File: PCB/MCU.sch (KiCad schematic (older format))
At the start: 17 parts, among them SW1 EG1224, U1 STM32F767VIT6

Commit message: Changed PCB.
- Added MOSFET, connectors sheet
- Changed MCU and power sheet
- Reorganised sheets
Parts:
- added C? (x2): 8pF, Capacitor_SMD:C_0603_1608Metric, symbol Device:C
- added C? (x4): 100nF, Capacitor_SMD:C_0603_1608Metric, symbol Device:C
- added C? (x2): C, Capacitor_SMD:C_0603_1608Metric, symbol Device:C
- added L? (x2): MPZ1608S221A, Resistor_SMD:R_0603_1608Metric, symbol Device:Ferrite_Bead_Small
- added R? (x4): 22, Resistor_SMD:R_0603_1608Metric, symbol Device:R
- added R? (x4): 1K, Resistor_SMD:R_0603_1608Metric, symbol Device:R
- added R?: 10k, Resistor_SMD:R_0603_1608Metric, symbol Device:R
- added SW?: PTS645VL39-2, Button_Switch_THT:SW_Tactile_SPST_Angled_PTS645Vx39-2LFS, symbol Switch:SW_Push
- added TP?: MCO, symbol Connector_Specialized:Test_Point
- added TP?: CLK24, symbol Connector_Specialized:Test_Point
- added U?: ADUM4160, Package_SO:SOIC-16W_7.5x10.3mm_P1.27mm, symbol Interface_USB:ADUM4160
- added U?: PCA9306, symbol Interface:PCA9306
- added Y?: TSX-3225 24.0000MF15X-AC3, Crystal:Crystal_SMD_SeikoEpson_TSX3225-4Pin_3.2x2.5mm, symbol Device:Crystal
- U?: renamed from U1; value STM32F767VIT6 -> STM32F765VIT6; symbol remram-custom:STM32F767VIT6 -> remram-custom:STM32F765VIT6
- renumbered C8 to C?, C11 to C?, C7 to C?, C10 to C?, C3 to C?, C4 to C?, C5 to C?, C6 to C?, C9 to C?, C12 to C?, C13 to C?, C14 to C?, C15 to C?, R1 to R?, R2 to R?, SW1 to SW?
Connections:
- net labels added: DD+, DD-, GNDS, M1_DIAG, M1_DIR, M1_EN, M1_STEP, M2_DIAG, M2_DIR, M2_EN, M2_STEP, M3_DIAG, M3_DIR, M3_EN, M3_STEP, M4_DIAG, M4_DIR, M4_EN, M4_STEP, MCU_BTN_EN1, MCU_BTN_EN2, MCU_BTN_ENC, MCU_DD+, MCU_DD-, MCU_EXT_D1, MCU_EXT_D2, MCU_EXT_D3, MCU_KILL_PIN, MCU_LCD_BEEPER, MCU_LCD_D4, MCU_LCD_D5, MCU_LCD_D6, MCU_LCD_D7, MCU_LCD_EN, MCU_LCD_RD, MCU_MISO, MCU_MOSI, MCU_SCK, MCU_SCL, MCU_SDA, MCU_SD_CARD_DET, MCU_SSM1, MCU_SSM2, MCU_SSM3, MCU_SSM4, MCU_SSSD, MCU_X_MAX, MCU_X_MIN, MCU_Y_MAX, MCU_Y_MIN, MCU_Z_MAX, MCU_Z_MIN, PWM_BED, PWM_FAN1, PWM_FAN2, PWM_HEAT, SCL, SDA, SWCLK, SWDIO, THERM_1, THERM_2, THERM_3, VBUS, VDD5V, nRESET
- net labels removed: +3.3V, NRESET
- wire segments 37 -> 110
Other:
- note added: "I2C Level Shifting"
- note added: "USB Isolation"
- note removed: "TODO:\n - RESET Button\n - 24MHz Crystall"
- moved on the sheet: C?, R?, SW?

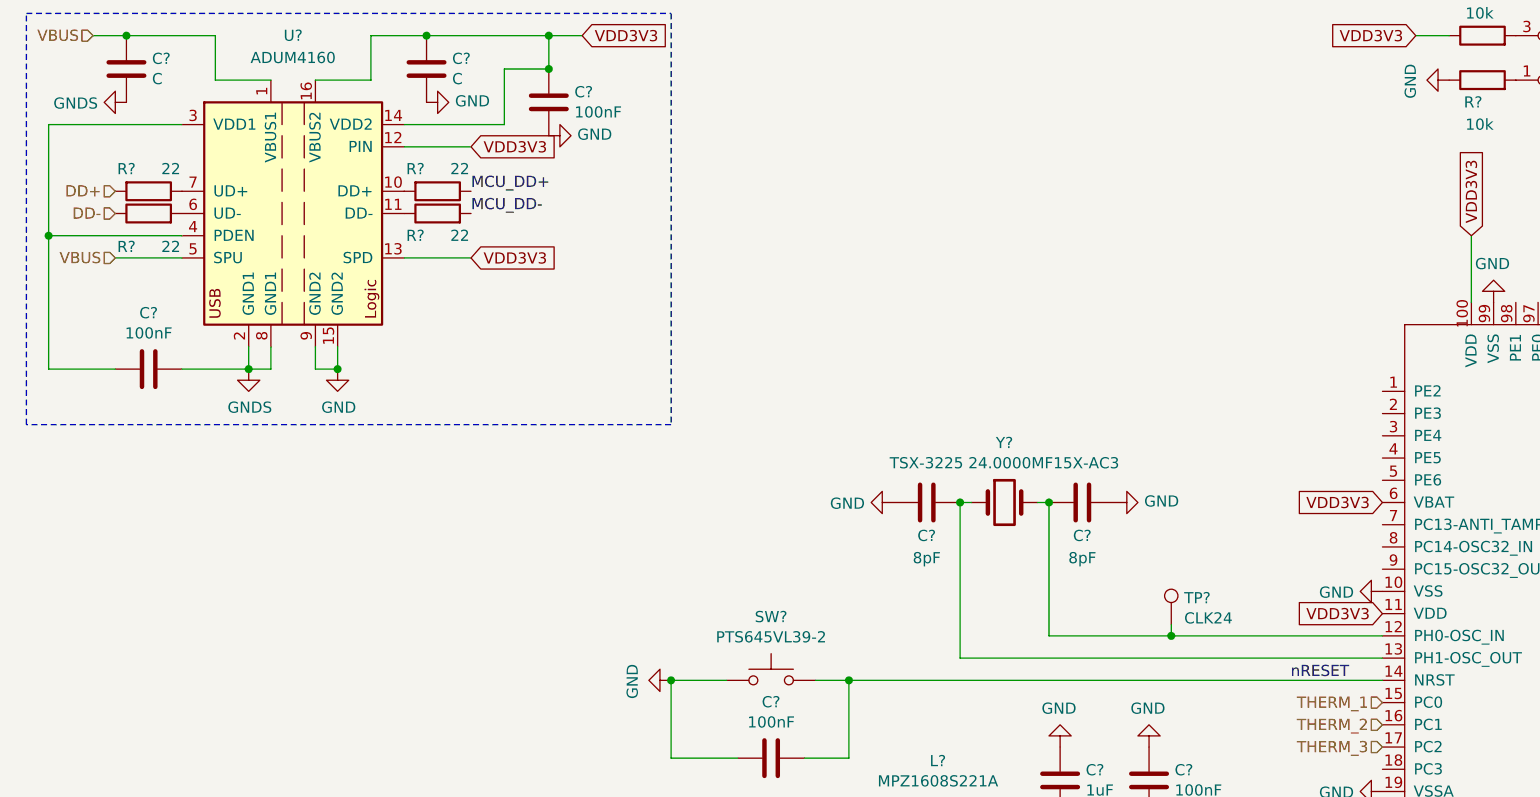
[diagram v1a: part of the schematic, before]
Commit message: Changed some sheets and added LICENCE.
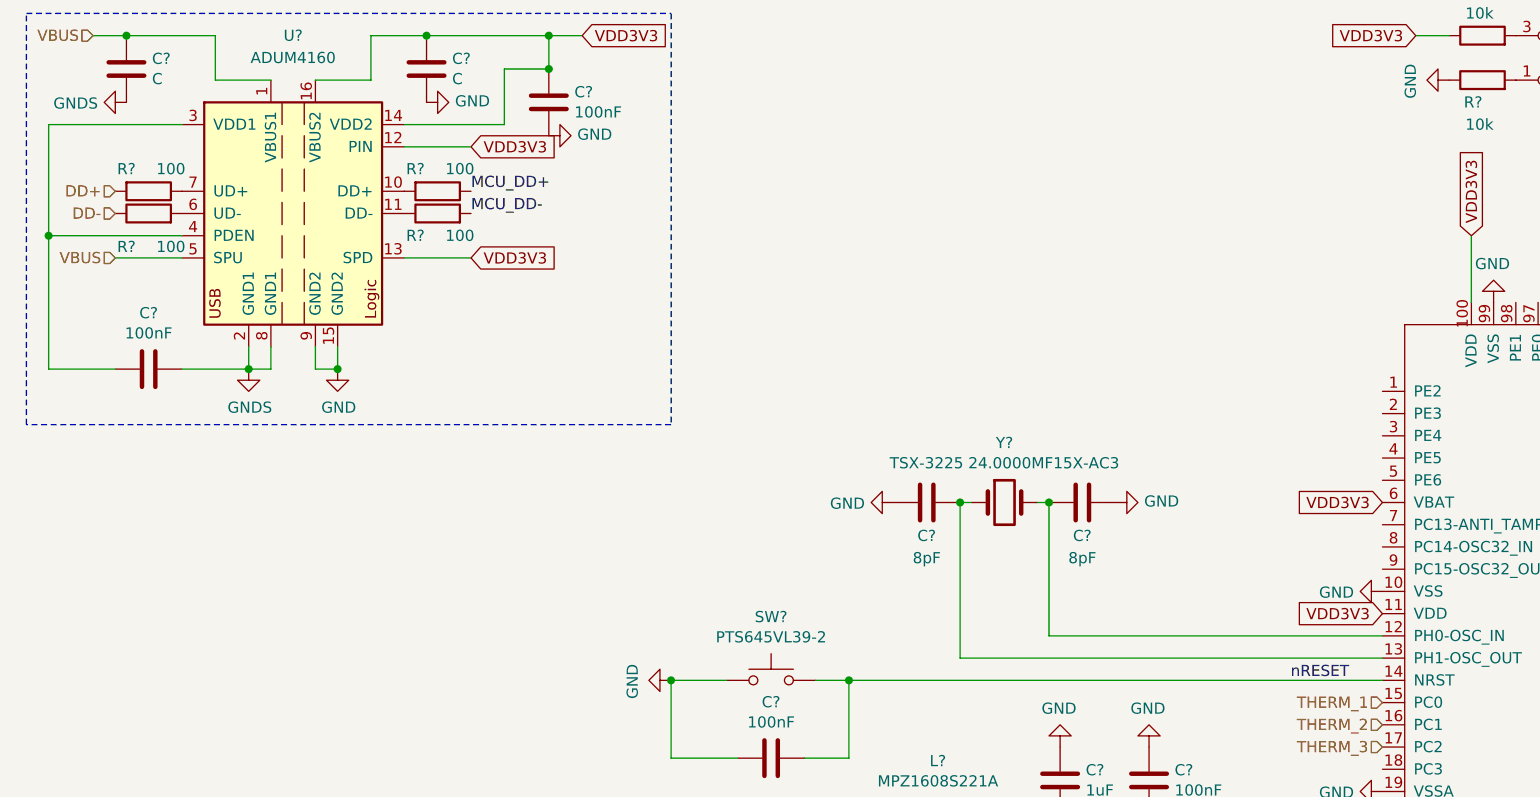
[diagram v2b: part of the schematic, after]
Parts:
- removed TP?: CLK24, symbol Connector_Specialized:Test_Point
- R? (x4): value 22 -> 100
- TP?: footprint (none) -> TestPoint:TestPoint_Pad_D1.0mm
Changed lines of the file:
@@
 P 2400 1550
 F 0 "R?" V 2300 1650 50  0000 C CNN
-F 1 "22" V 2300 1450 50  0000 C CNN
+F 1 "100" V 2300 1450 50  0000 C CNN
 F 2 "Resistor_SMD:R_0603_1608Metric" V 2330 1550 50  0001 C CNN
 F 3 "~" H 2400 1550 50  0001 C CNN
@@
 P 2400 1450
 F 0 "R?" V 2300 1350 50  0000 C CNN
-F 1 "22" V 2300 1550 50  0000 C CNN
+F 1 "100" V 2300 1550 50  0000 C CNN
 F 2 "Resistor_SMD:R_0603_1608Metric" V 2330 1450 50  0001 C CNN
 F 3 "~" H 2400 1450 50  0001 C CNN
@@
 P 1100 1550
 F 0 "R?" V 950 1650 50  0000 C CNN
-F 1 "22" V 950 1450 50  0000 C CNN
+F 1 "100" V 950 1450 50  0000 C CNN
 F 2 "Resistor_SMD:R_0603_1608Metric" V 1030 1550 50  0001 C CNN
 F 3 "~" H 1100 1550 50  0001 C CNN
@@
 P 1100 1450
 F 0 "R?" V 1000 1350 50  0000 C CNN
-F 1 "22" V 1000 1550 50  0000 C CNN
+F 1 "100" V 1000 1550 50  0000 C CNN
 F 2 "Resistor_SMD:R_0603_1608Metric" V 1030 1450 50  0001 C CNN
 F 3 "~" H 1100 1450 50  0001 C CNN
@@
 F 0 "TP?" H 10658 3270 50  0000 L CNN
 F 1 "MCO" H 10658 3179 50  0000 L CNN
-F 2 "" H 10800 3150 50  0001 C CNN
+F 2 "TestPoint:TestPoint_Pad_D1.0mm" H 10800 3150 50  0001 C CNN
 F 3 "~" H 10800 3150 50  0001 C CNN
 	1    10600 3150
 	1    0    0    -1
 $EndComp
-$Comp
-L Connector_Specialized:Test_Point TP?
-U 1 1 5B138091
-P 5700 3400
-F 0 "TP?" H 5758 3520 50  0000 L CNN
-F 1 "CLK24" H 5758 3429 50  0000 L CNN
-F 2 "" H 5900 3400 50  0001 C CNN
-F 3 "~" H 5900 3400 50  0001 C CNN
-	1    5700 3400
-	1    0    0    -1
-$EndComp
-Wire Wire Line
-	5700 3400 5700 3450
-Wire Wire Line
-	5150 3450 5700 3450
-Connection ~ 5700 3450
-Wire Wire Line
-	5700 3450 6650 3450
 Text Label 2550 1450 0    50   ~ 0
 MCU_DD+
@@
 Text HLabel 6650 4550 0    50   Output ~ 0
 PWM_HEAT
+Wire Wire Line
+	5150 3450 6650 3450
 $EndSCHEMATC

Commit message: Finished first draft of the schematics.
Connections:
- net M1_DIAG renamed X_DIAG
- net M1_DIR renamed X_DIR
- net M1_EN renamed X_EN
- net M1_STEP renamed X_STEP
- net M2_DIAG renamed Y_DIAG
- net M2_DIR renamed Y_DIR
- net M2_EN renamed Y_EN
- net M2_STEP renamed Y_STEP
- net M3_DIAG renamed Z_DIAG
- net M3_DIR renamed Z_DIR
- net M3_EN renamed Z_EN
- net M3_STEP renamed Z_STEP
- net M4_DIAG renamed E_DIAG
- net M4_DIR renamed E_DIR
- net M4_EN renamed E_EN
- net M4_STEP renamed E_STEP
- net MCU_SSM1 renamed MCU_SSX
- net MCU_SSM2 renamed MCU_SSY
- net MCU_SSM3 renamed MCU_SSZ
- net MCU_SSM4 renamed MCU_SSE
- no-connect marks 0 -> 21
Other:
- moved on the sheet: C?, SW?
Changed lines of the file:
@@
 $Descr A4 11693 8268
 encoding utf-8
-Sheet 2 5
+Sheet 2 9
 Title "MCU"
 Date ""
@@
 L Switch:SW_Push SW?
 U 1 1 5AF60A7F
-P 3900 3650
-F 0 "SW?" H 3900 3935 50  0000 C CNN
-F 1 "PTS645VL39-2" H 3900 3844 50  0000 C CNN
-F 2 "Button_Switch_THT:SW_Tactile_SPST_Angled_PTS645Vx39-2LFS" H 3900 3850 50  0001 C CNN
-F 3 "https://www.mouser.de/datasheet/2/60/-1131575.pdf" H 3900 3850 50  0001 C CNN
-	1    3900 3650
+P 3350 3650
+F 0 "SW?" H 3350 3935 50  0000 C CNN
+F 1 "PTS645VL39-2" H 3350 3844 50  0000 C CNN
+F 2 "Button_Switch_THT:SW_Tactile_SPST_Angled_PTS645Vx39-2LFS" H 3350 3850 50  0001 C CNN
+F 3 "https://www.mouser.de/datasheet/2/60/-1131575.pdf" H 3350 3850 50  0001 C CNN
+	1    3350 3650
 	1    0    0    -1
 $EndComp
@@
 L power:GND #PWR?
 U 1 1 5AF616AA
-P 3450 3650
-F 0 "#PWR?" H 3450 3400 50  0001 C CNN
-F 1 "GND" H 3455 3477 50  0000 C CNN
-F 2 "" H 3450 3650 50  0001 C CNN
-F 3 "" H 3450 3650 50  0001 C CNN
-	1    3450 3650
-	0    1    1    0
-$EndComp
-Wire Wire Line
-	3450 3650 3700 3650
+P 2900 3650
+F 0 "#PWR?" H 2900 3400 50  0001 C CNN
+F 1 "GND" H 2905 3477 50  0000 C CNN
+F 2 "" H 2900 3650 50  0001 C CNN
+F 3 "" H 2900 3650 50  0001 C CNN
+	1    2900 3650
+	0    1    1    0
+$EndComp
+Wire Wire Line
+	2900 3650 3150 3650
 $Comp
 L Device:C C?
 U 1 1 5AF62329
-P 3900 4000
-F 0 "C?" V 4152 4000 50  0000 C CNN
-F 1 "100nF" V 4061 4000 50  0000 C CNN
-F 2 "Capacitor_SMD:C_0603_1608Metric" H 3938 3850 50  0001 C CNN
-F 3 "~" H 3900 4000 50  0001 C CNN
-	1    3900 4000
+P 3350 4000
+F 0 "C?" V 3602 4000 50  0000 C CNN
+F 1 "100nF" V 3511 4000 50  0000 C CNN
+F 2 "Capacitor_SMD:C_0603_1608Metric" H 3388 3850 50  0001 C CNN
+F 3 "~" H 3350 4000 50  0001 C CNN
+	1    3350 4000
 	0    -1   -1   0
 $EndComp
 Wire Wire Line
-	4050 4000 4250 4000
-Wire Wire Line
-	4250 3650 4100 3650
-Wire Wire Line
-	3450 3650 3450 4000
-Wire Wire Line
-	3450 4000 3750 4000
+	3500 4000 3700 4000
+Wire Wire Line
+	2900 3650 2900 4000
+Wire Wire Line
+	2900 4000 3200 4000
 $Comp
 L power:GND #PWR?
@@
 	4850 4350 5200 4350
 Connection ~ 5200 4350
-Text Label 6500 3650 2    50   ~ 0
-nRESET
 Text HLabel 6650 3750 0    50   Input ~ 0
 THERM_1
@@
 MCU_SCL
 Text HLabel 9050 5150 3    50   Output ~ 0
-M3_STEP
+Z_STEP
 Text HLabel 9150 5150 3    50   Output ~ 0
-M4_STEP
-Connection ~ 3450 3650
-Wire Wire Line
-	4250 3650 4250 4000
-Connection ~ 4250 3650
+E_STEP
+Connection ~ 2900 3650
 $Comp
 L remram-custom:STM32F765VIT6 U?
@@
 MCU_DD-
 Text HLabel 9150 1950 1    50   Output ~ 0
-M1_EN
+X_EN
 Text HLabel 9250 1950 1    50   Output ~ 0
-M1_DIR
+X_DIR
 Text HLabel 9050 1950 1    50   Input ~ 0
-M1_DIAG
+X_DIAG
 Text HLabel 9350 1950 1    50   Output ~ 0
-M1_STEP
+X_STEP
 Text HLabel 8150 1950 1    50   Output ~ 0
-M2_STEP
+Y_STEP
 Text HLabel 8350 1950 1    50   Output ~ 0
-M2_EN
+Y_EN
 Text HLabel 8250 1950 1    50   Output ~ 0
-M2_DIR
+Y_DIR
 Text HLabel 8450 1950 1    50   Input ~ 0
-M2_DIAG
+Y_DIAG
 Text HLabel 8550 5150 3    50   Output ~ 0
-M3_EN
+Z_EN
 Text HLabel 8650 5150 3    50   Output ~ 0
-M3_DIR
+Z_DIR
 Text HLabel 8450 5150 3    50   Input ~ 0
-M3_DIAG
+Z_DIAG
 Text GLabel 9850 2350 2    50   Input ~ 0
 VDD3V3
 Text HLabel 8850 5150 3    50   Output ~ 0
-M4_EN
+E_EN
 Text HLabel 8950 5150 3    50   Output ~ 0
-M4_DIR
+E_DIR
 Text HLabel 8750 5150 3    50   Input ~ 0
-M4_DIAG
+E_DIAG
 Wire Wire Line
 	7050 5150 7050 5250
@@
 	5600 4250 6650 4250
 Connection ~ 5600 4250
-Wire Wire Line
-	4250 3650 6650 3650
 Wire Wire Line
 	7650 850  7650 1950
@@
 MCU_MOSI
 Text HLabel 7650 5150 3    50   Output ~ 0
-MCU_SSM1
+MCU_SSX
 Text HLabel 7750 5150 3    50   Output ~ 0
-MCU_SSM2
+MCU_SSY
 Text HLabel 7850 5150 3    50   Output ~ 0
-MCU_SSM3
+MCU_SSZ
 Text HLabel 7950 5150 3    50   Output ~ 0
-MCU_SSM4
+MCU_SSE
 Text HLabel 8050 5150 3    50   Output ~ 0
 MCU_SSSD
@@
 Wire Wire Line
 	5150 3450 6650 3450
+NoConn ~ 6650 2350
+NoConn ~ 6650 2450
+NoConn ~ 6650 2550
+NoConn ~ 6650 2650
+NoConn ~ 6650 2750
+NoConn ~ 6650 2950
+NoConn ~ 6650 3050
+NoConn ~ 6650 3150
+NoConn ~ 6650 4050
+NoConn ~ 7250 5150
+NoConn ~ 8950 1950
+NoConn ~ 8850 1950
+NoConn ~ 8750 1950
+NoConn ~ 8650 1950
+NoConn ~ 8550 1950
+NoConn ~ 8050 1950
+NoConn ~ 7950 1950
+NoConn ~ 7550 1950
+NoConn ~ 7450 1950
+NoConn ~ 7350 1950
+NoConn ~ 7250 1950
+Text HLabel 3700 3150 0    50   Input ~ 0
+nRESET
+Wire Wire Line
+	4250 3650 6650 3650
+Wire Wire Line
+	3700 3150 4250 3150
+Wire Wire Line
+	4250 3150 4250 3650
+Wire Wire Line
+	3550 3650 3700 3650
+Connection ~ 4250 3650
+Wire Wire Line
+	3700 4000 3700 3650
+Connection ~ 3700 3650
+Wire Wire Line
+	3700 3650 4250 3650
 $EndSCHEMATC

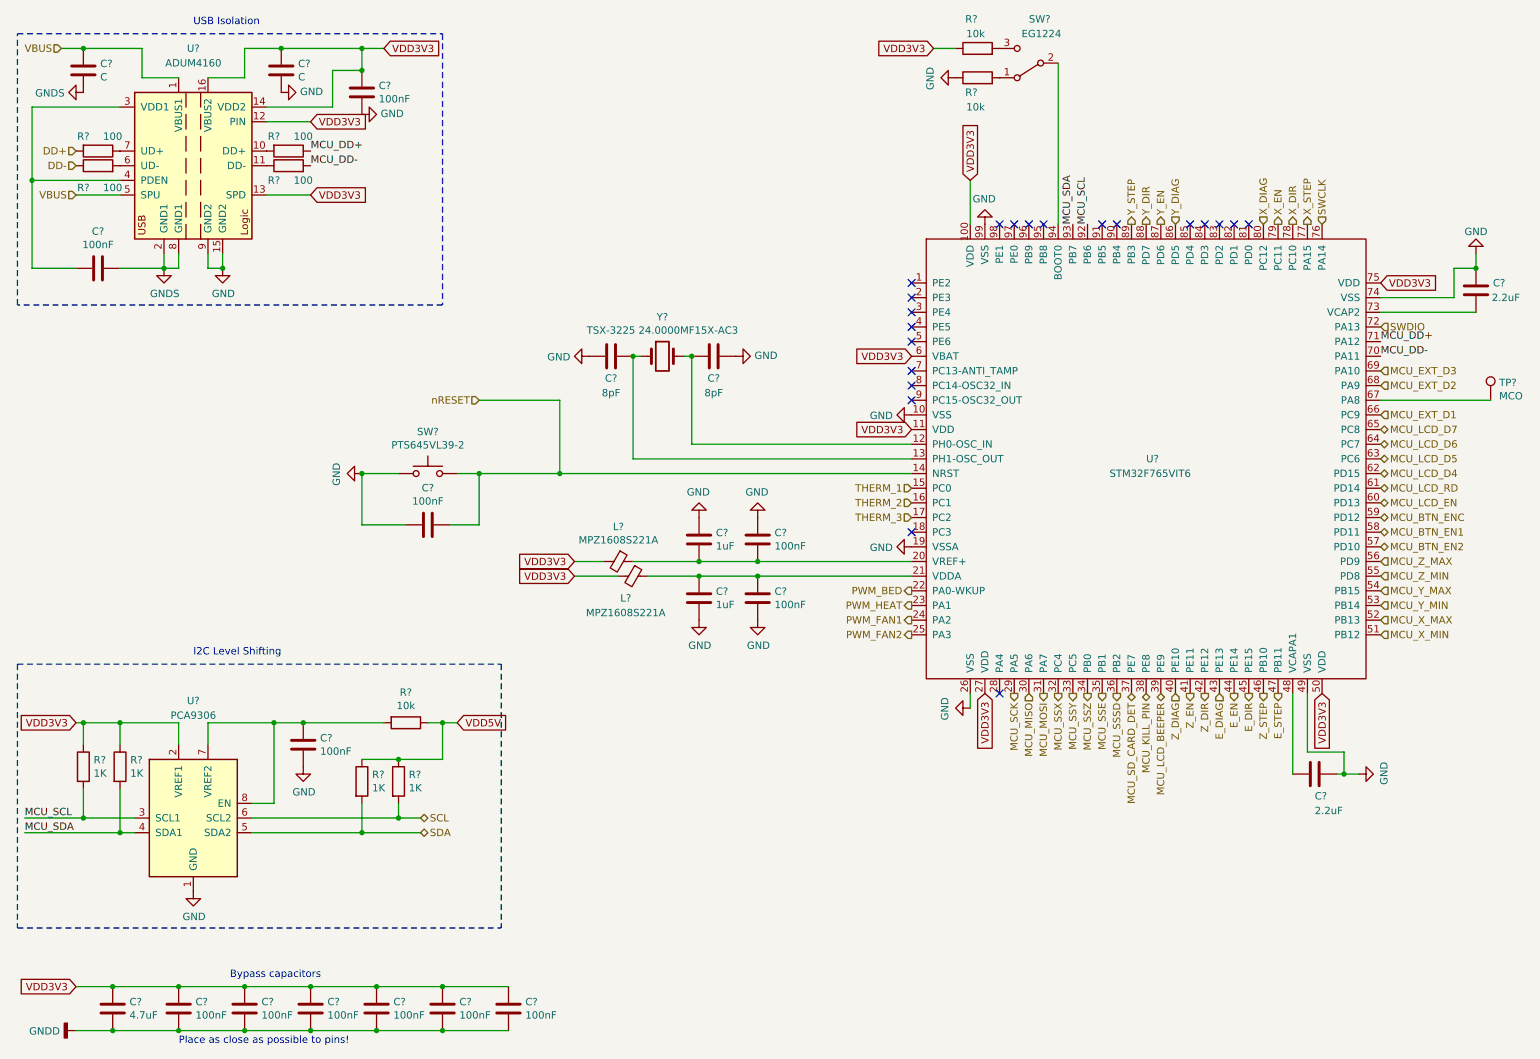
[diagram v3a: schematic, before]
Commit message: Fixed bugs found with ERC.
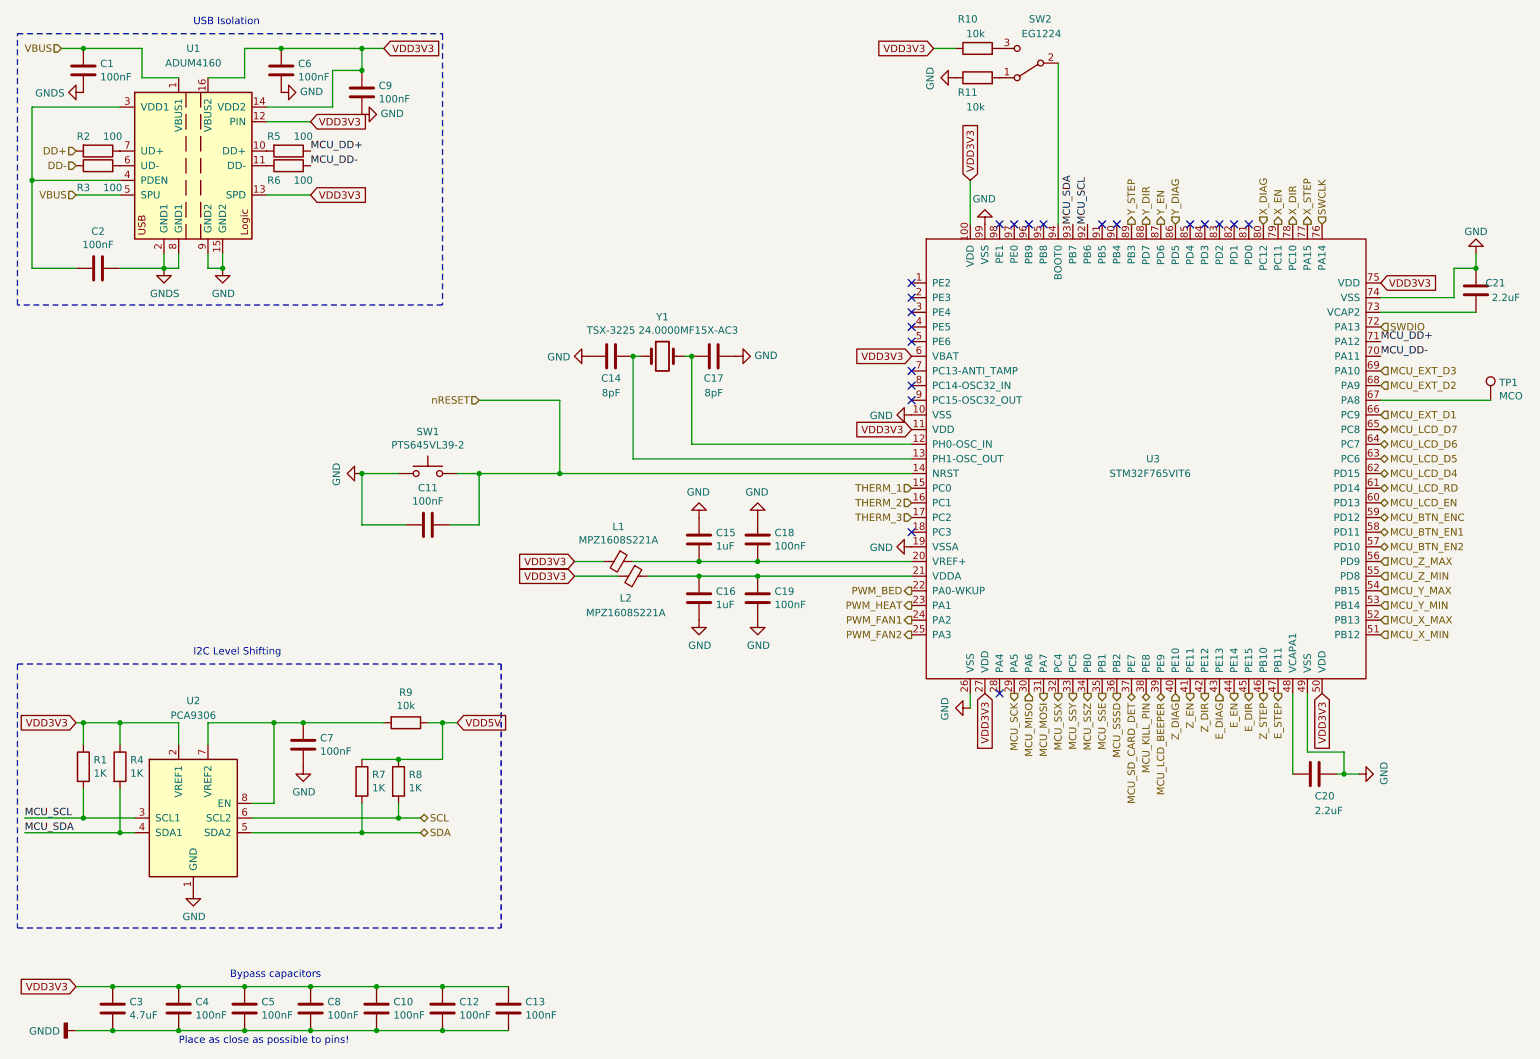
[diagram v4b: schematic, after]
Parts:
- C1, C6: renamed from C?; value C -> 100nF
- gave numbers to parts that had none: 39
